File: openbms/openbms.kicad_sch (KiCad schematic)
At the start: 0 parts

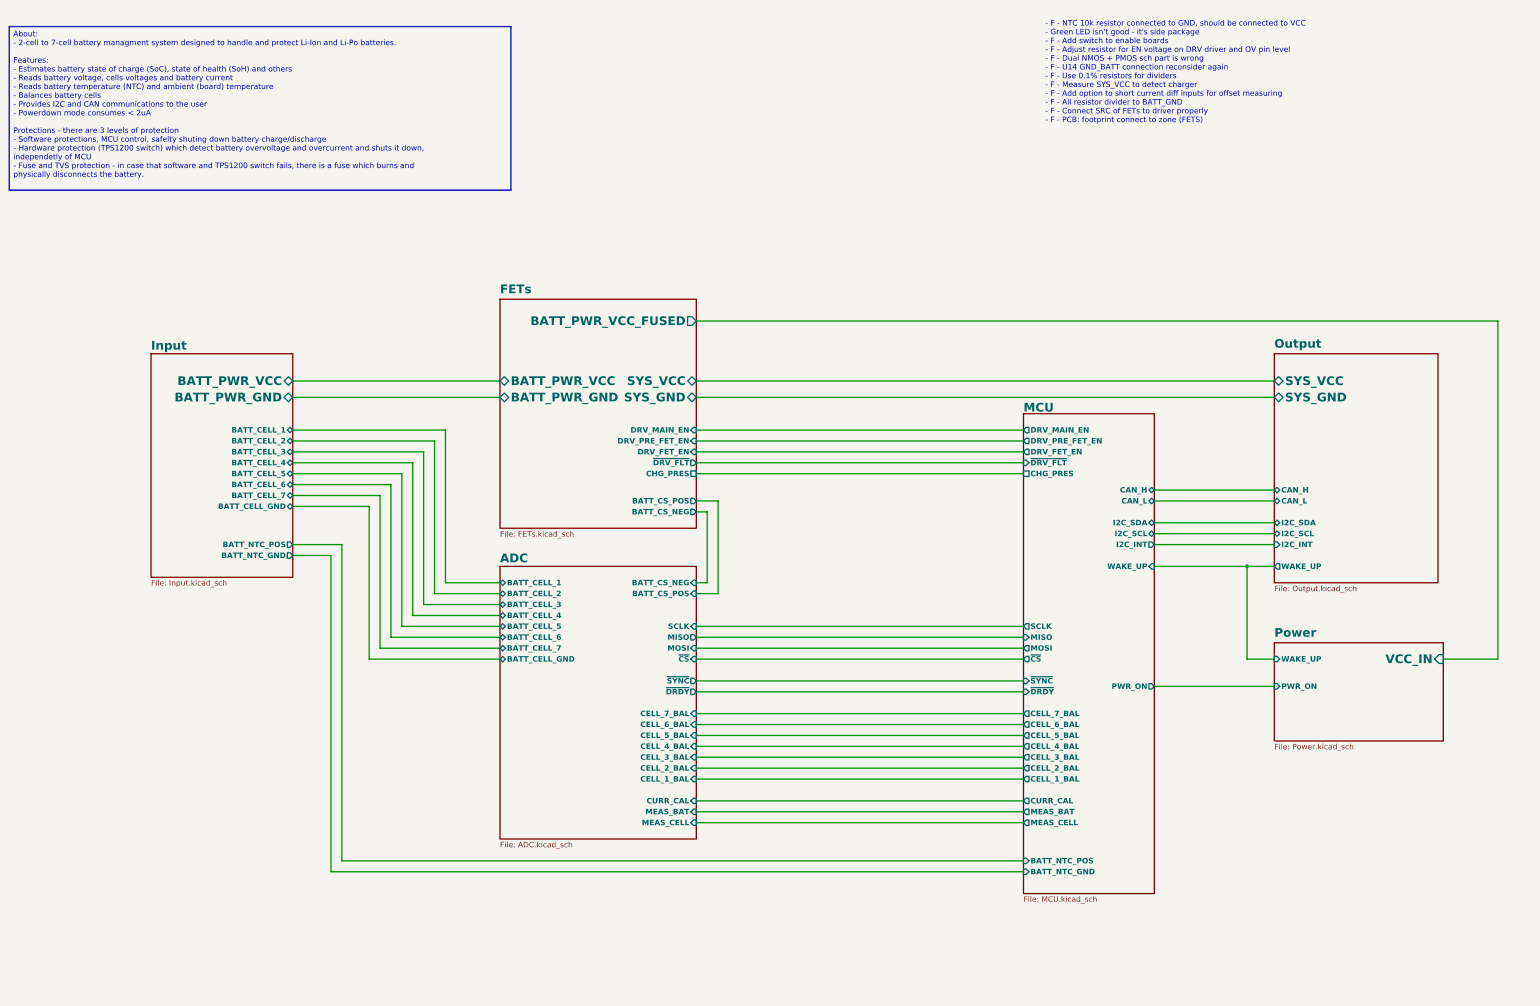
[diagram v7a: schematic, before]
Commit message: Revision B comments added, PDF generated
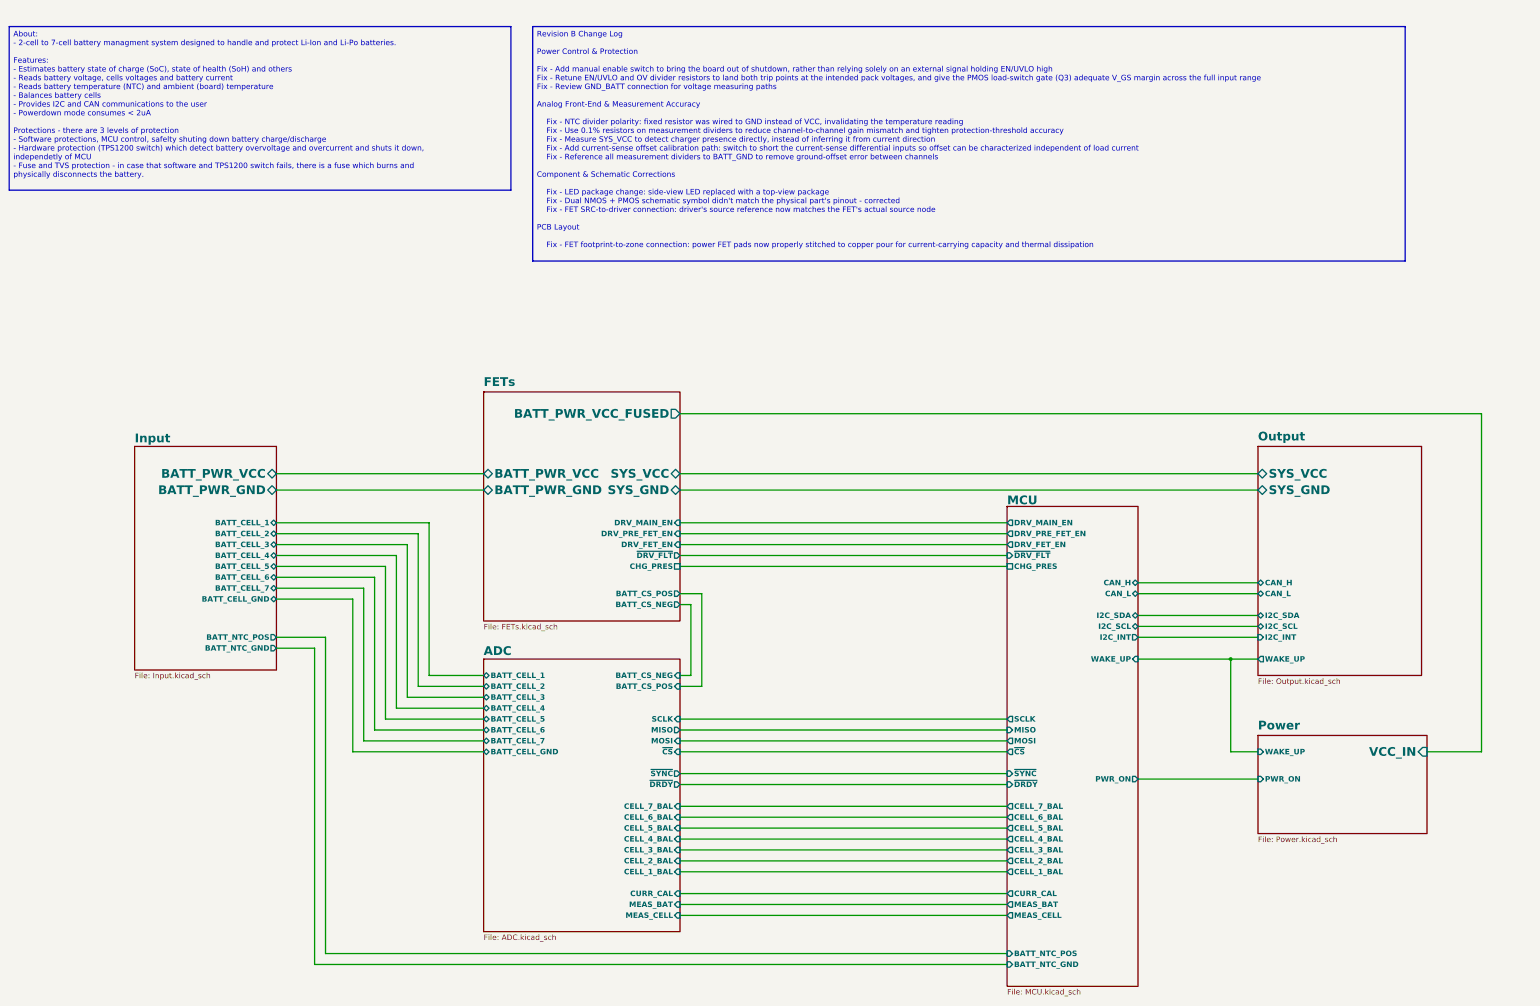
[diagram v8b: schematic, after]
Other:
- note removed: "- F - NTC 10k resistor connected to GND, should be connected to VCC - Green LED isn't good - it's side package - F - Add switch to enable boards - F - Adjust resistor for EN voltage on DRV driver and OV pin level - F - Dual NMOS + PMOS sch part is wrong - F - U14 GND_BATT connection reconsider again - F - Use 0.1% resistors for dividers - F - Measure SYS_VCC to detect charger - F - Add option to 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"
